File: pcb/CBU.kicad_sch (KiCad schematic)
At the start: 54 parts, among them J1 Conn_01x03_Socket, J11 Conn_01x03_Pin, J4 Conn_01x02_Socket, J5 Conn_01x02_Socket, J6 Conn_01x03_Socket, J7 Conn_01x03_Socket, J9 USB_C_Receptacle, Q1 AO3416A, Q2 AO3416A, Q3 AO3416A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

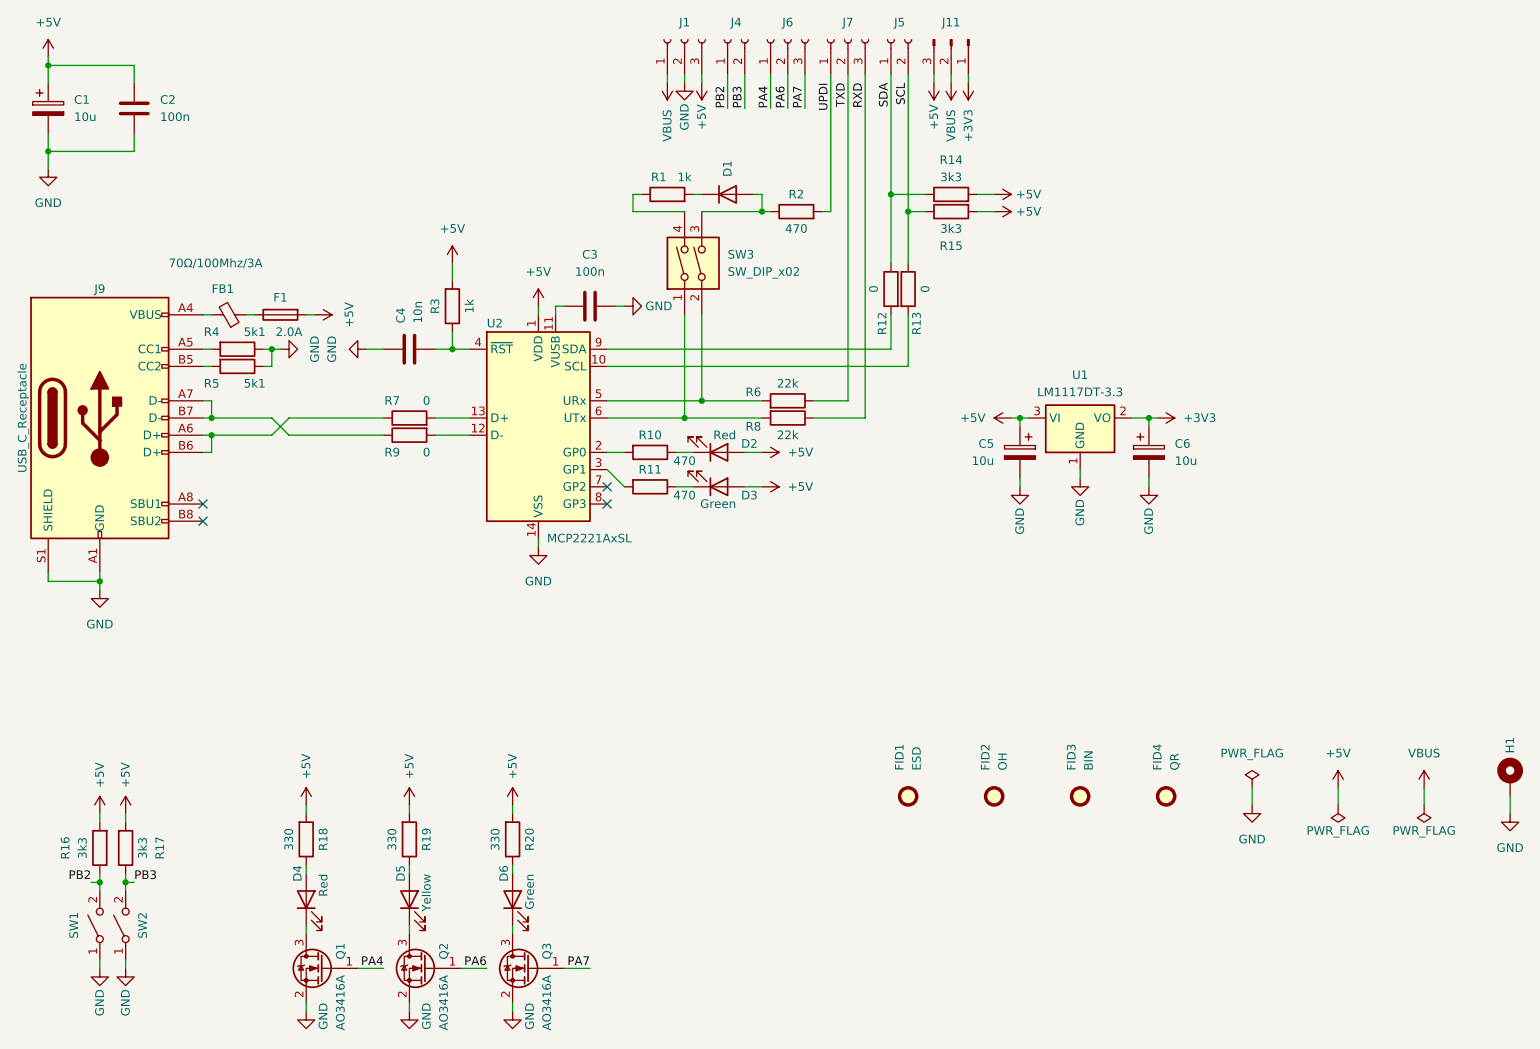
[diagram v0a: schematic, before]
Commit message: Change MCP2221A to FT230X
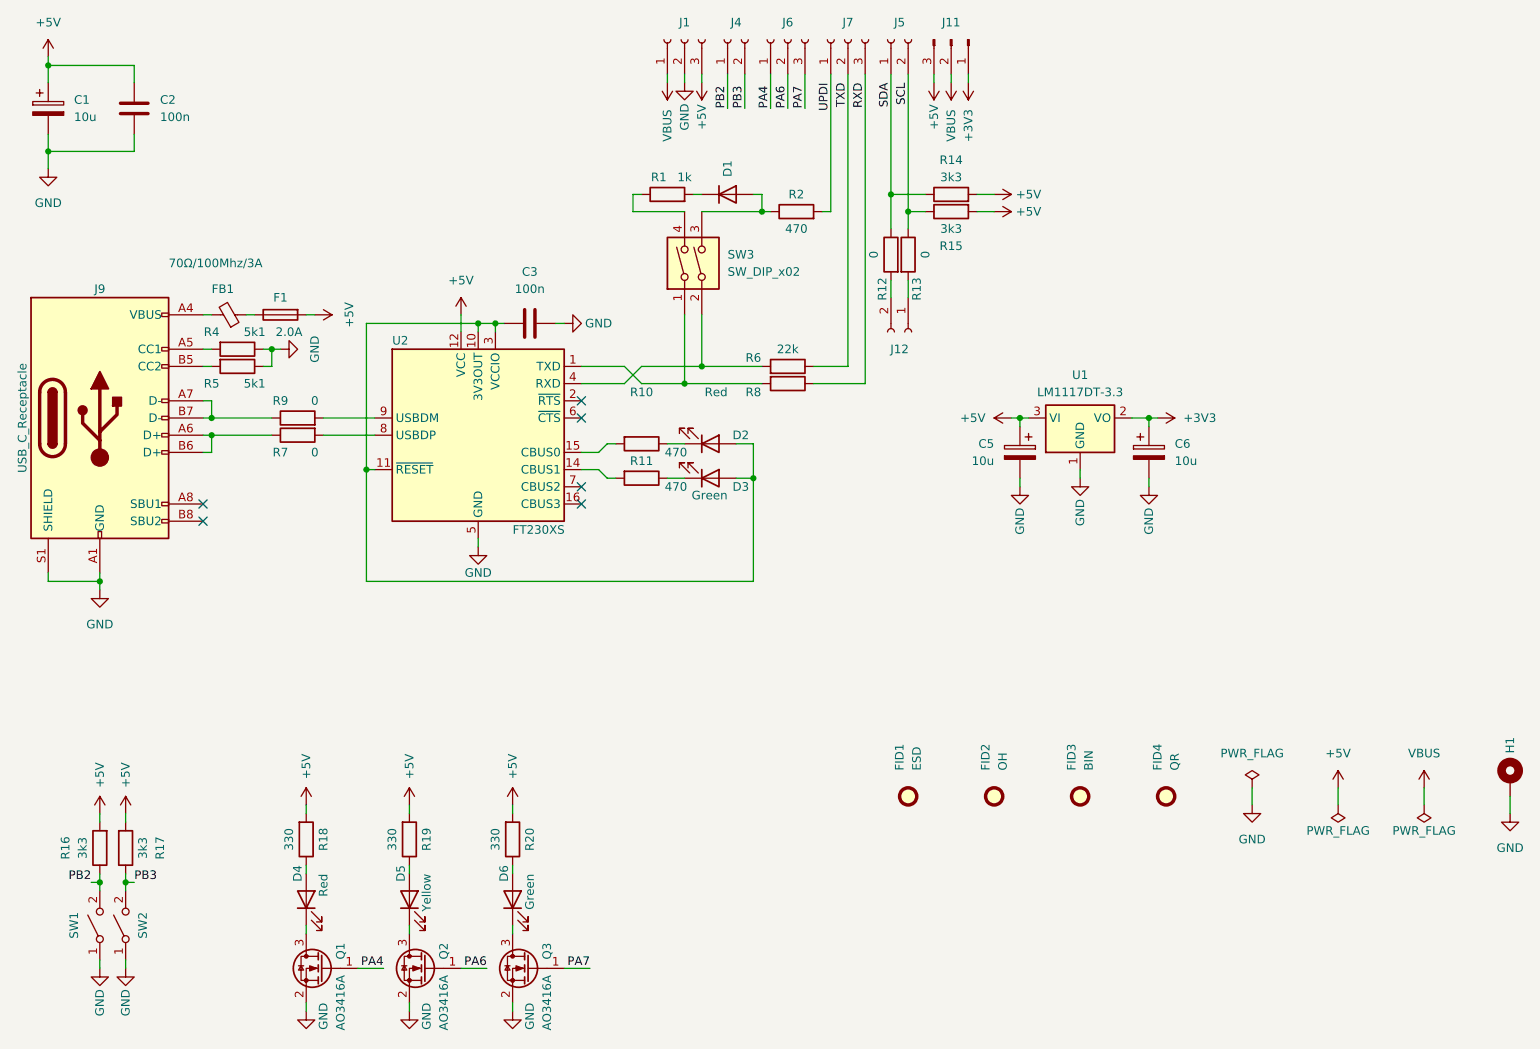
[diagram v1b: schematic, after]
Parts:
- removed C4: 10n, Capacitor_SMD:C_1206_3216Metric, symbol Device:C
- removed R3: 1k, Resistor_SMD:R_1206_3216Metric, symbol Device:R
- removed U2: MCP2221AxSL, Package_SO:SOIC-14_3.9x8.7mm_P1.27mm, symbol Interface_USB:MCP2221AxSL
- added J12: Conn_01x02_Socket, Connector_PinSocket_2.54mm:PinSocket_1x02_P2.54mm_Vertical, symbol Connector:Conn_01x02_Socket
- added U2: FT230XS, Package_SO:SSOP-16_3.9x4.9mm_P0.635mm, symbol Interface_USB:FT230XS
- C3: HTL (none) -> 100128
- D2: HTL (none) -> 100458
- D3: HTL (none) -> 100459
- FID1, FID2, FID3, FID4: now left out of the parts list
- R10, R11: HTL (none) -> 102944
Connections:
- net +5V: now also U2.12 (VCC); no longer D2.2 (A), D3.2 (A)
- net GND: now also U2.13 (GND), U2.5 (GND)
- net at R10.2: now also U2.15 (CBUS0)
- net at R11.2: now also U2.14 (CBUS1)
- net at R8.2, SW3.1: now also U2.1 (TXD)
- net at R6.2, SW3.2: now also U2.4 (RXD)
- net at R12.2: now also J12.2 (Pin_2)
- net at C3.1: now also D2.2 (A), D3.2 (A), U2.10 (3V3OUT), U2.11 (~{RESET}), U2.3 (VCCIO)
- net at R13.2: now also J12.1 (Pin_1)
- net at R7.2: now also U2.8 (USBDP)
- net at R9.2: now also U2.9 (USBDM)
- no-connect marks 4 -> 6
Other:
- moved on the sheet: R12, R13, R6, R7, R8, R9

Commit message: Rename/Add/Remove bom fields
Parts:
- C1: HTL (none) -> 103620; Vendor HTL -> (none); VendorId 103620 -> (none)
- C2: HTL (none) -> 100128; Vendor HTL -> (none); VendorId 100128 -> (none)
- C3: Vendor HTL -> (none); VendorId 100128 -> (none)
- C5, C6: DigiKey (none) -> 732-8545-1-ND; Vendor DigiKey -> (none); VendorId 732-8545-1-ND -> (none)
- D1: HTL (none) -> 100206; Vendor HTL -> (none); VendorId 100206 -> (none)
- D2: Vendor HTL -> (none); VendorId 100458 -> (none)
- D3: Vendor HTL -> (none); VendorId 100459 -> (none)
- D4: HTL (none) -> 100458; Vendor HTL -> (none); VendorId 100458 -> (none)
- D5: HTL (none) -> 100457; Vendor HTL -> (none); VendorId 100457 -> (none)
- D6: HTL (none) -> 100459; Vendor HTL -> (none); VendorId 100459 -> (none)
- F1: HTL (none) -> 103597; Vendor HTL -> (none); VendorId 103597 -> (none)
- FB1: HTL (none) -> 103570; Vendor HTL -> (none); VendorId 103570 -> (none)
- J1, J6, J7: DigiKey (none) -> 2057-RS1-03-G-ND; Vendor DigiKey -> (none); VendorId 2057-RS1-03-G-ND -> (none)
- J11: HTL (none) -> 101521; Vendor HTL -> (none); VendorId 101521 -> (none)
- J12, J4, J5: DigiKey (none) -> 2057-RS1-02-G-ND; Vendor DigiKey -> (none); VendorId 2057-RS1-02-G-ND -> (none)
- J9: HTL (none) -> 103572; Vendor HTL -> (none); VendorId 103572 -> (none)
- Q1, Q2, Q3: HTL (none) -> 103512; Vendor HTL -> (none); VendorId 103512 -> (none)
- R1: HTL (none) -> 102951; Vendor HTL -> (none); VendorId 102951 -> (none)
- R10, R11: Vendor HTL -> (none); VendorId 102944 -> (none)
- R12, R13: HTL (none) -> 102902; Vendor HTL -> (none); VendorId 102902 -> (none)
- R14, R15, R16, R17: HTL (none) -> 102959; Vendor HTL -> (none); VendorId 102959 -> (none)
- R18, R19, R20: HTL (none) -> 102940; Vendor HTL -> (none); VendorId 102940 -> (none)
- R2: HTL (none) -> 102944; Vendor HTL -> (none); VendorId 102944 -> (none)
- R4, R5: HTL (none) -> 102962; Vendor HTL -> (none); VendorId 102962 -> (none)
- R6, R8: HTL (none) -> 102973; Vendor HTL -> (none); VendorId 102973 -> (none)
- R7, R9: DigiKey (none) -> RMCF0603ZT0R00CT-ND; Vendor DigiKey -> (none); VendorId RMCF0603ZT0R00CT-ND -> (none)
- SW1, SW2: HTL (none) -> 101614; Vendor HTL -> (none); VendorId 101614 -> (none)
- SW3: HTL (none) -> 103604; Vendor HTL -> (none); VendorId 103604 -> (none)
- U1: HTL (none) -> 103444; Vendor HTL -> (none); VendorId 103444 -> (none)
- U2: Vendor HTL -> (none); VendorId 103368 -> (none)
